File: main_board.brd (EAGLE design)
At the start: 160 x 100 mm, 8 parts, among them U1 MAX9019EKA+T

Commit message: working on the solar circuit
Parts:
- added C2: 10uF, MF_Passives:C0603
- added C3: 22uF, MF_Passives:C0603
- added J1: TBL009-254-02GY-2GY, PP_Connectors:TBL009-254-02GY-2GY
- added L1: 10uH, PP_Passives:LPS4012
- added R10, R7, R8, R9: (no value), MF_Passives:R0805
- added U2: AEM10941-QFN, PP_PowerIC:AEM10941_QFN-28
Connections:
- new net BOOST: C3.P$1, U2.P$1
- new net BUFSRC: C2.P$1, L1.P$2, U2.P$27
- new net SET_CHRDY: R8.P$2, R9.P$1, U2.P$23
- new net SET_OVCH: R10.P$1, R9.P$2, U2.P$22
- new net SET_OVDIS: R7.P$2, R8.P$1, U2.P$24
- new net SOLAR_+V: J1.1A, J1.1B, U2.P$25, U2.P$26
- new net SWBOOST: L1.P$1, U2.P$28
- new net VBOOST: R7.P$1
- net GND: now also C2.P$2, C3.P$2, J1.2A, J1.2B, R10.P$2

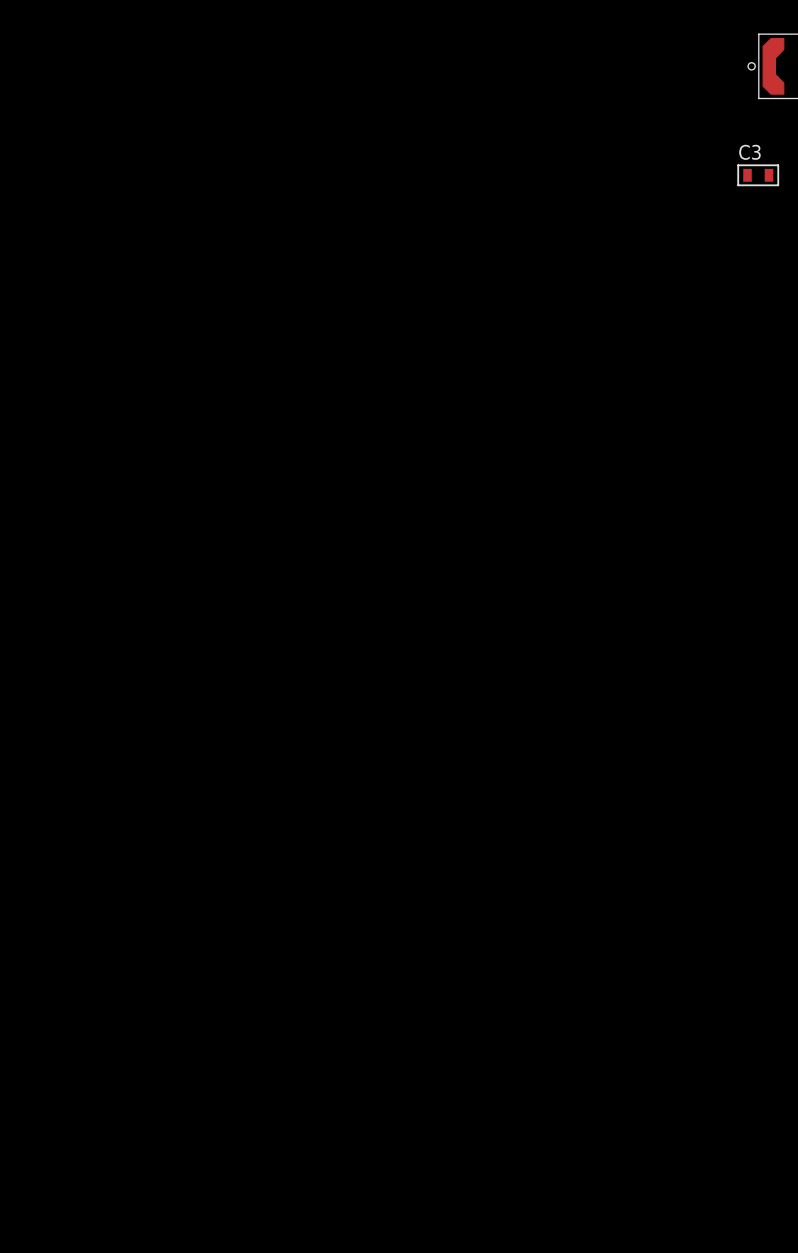
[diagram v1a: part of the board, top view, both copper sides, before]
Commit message: AEM10941 circuit complete
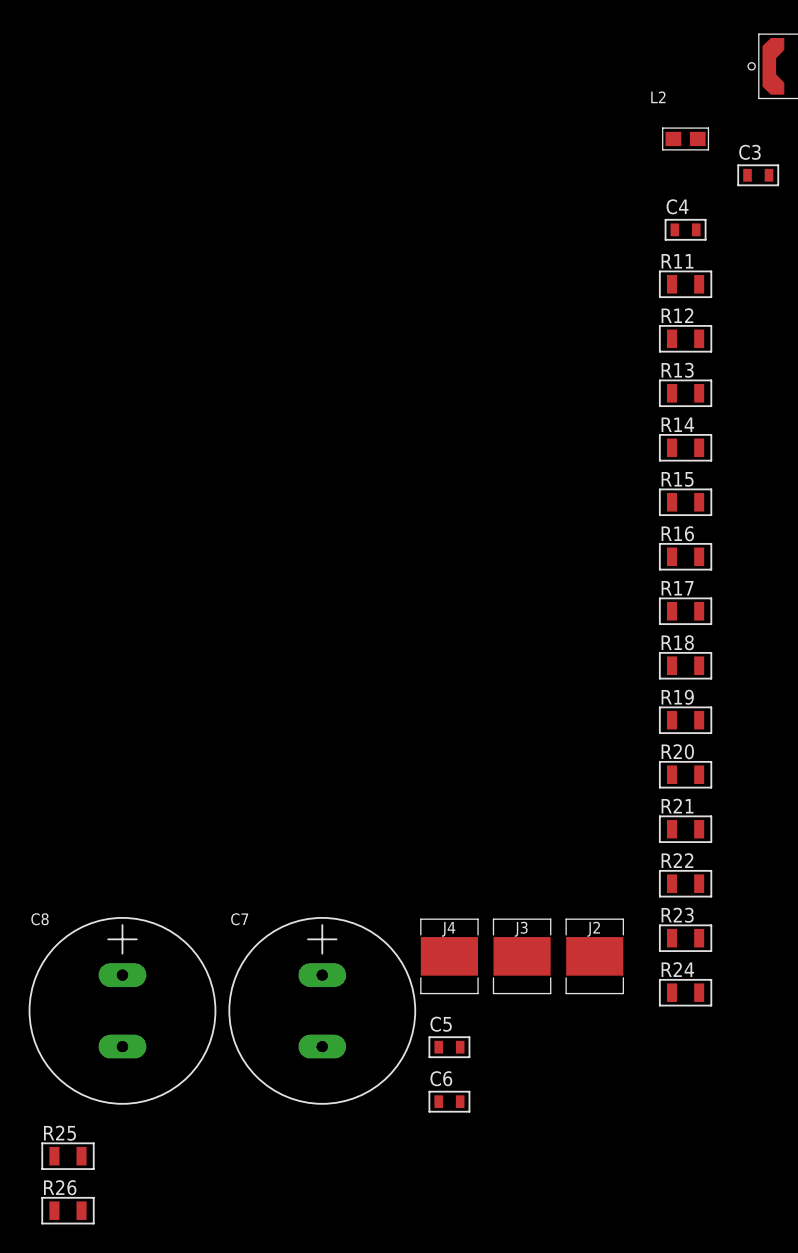
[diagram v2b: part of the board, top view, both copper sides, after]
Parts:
- added C4, C5, C6: 10uF, MF_Passives:C0603
- added C7, C8: 10F 3.8V, PP_Passives:12.5MM_CAP_PTH
- added J2, J3, J4: 709176001501006, PP_Connectors:709176001501006
- added L2: 10uH, PP_Passives:0603
- added R11, R12, R13, R14, R15, R16, R17, R18, R19, R20, R21, R22, R23, R24, R25, R26: (no value), MF_Passives:R0805
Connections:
- removed net BOOST: C3.P$1, U2.P$1
- new net BAL: C7.NEG, C8.POS, U2.P$15
- new net BATT: C7.POS, U2.P$16
- new net CFG[0]: R15.P$1, R16.P$2, U2.P$6
- new net CFG[1]: R13.P$1, R14.P$2, U2.P$5
- new net CFG[2]: R11.P$1, R12.P$2, U2.P$4
- new net ENHV: R21.P$1, R22.P$2, U2.P$12
- new net ENLV: R23.P$1, R24.P$2, U2.P$18
- new net FB_HV: R25.P$1, R26.P$2, U2.P$13
- new net HVOUT: C6.P$1, R25.P$2, U2.P$14
- new net LVOUT: C5.P$1, U2.P$11
- new net SELMPP[0]: R19.P$1, R20.P$2, U2.P$8
- new net SELMPP[1]: R17.P$1, R18.P$2, U2.P$7
- new net STATUS[0]: J4.P$1, U2.P$21
- new net STATUS[1]: J3.P$1, U2.P$20
- new net STATUS[2]: J2.P$1, U2.P$19
- new net SWBUCK: L2.1, U2.P$2
- new net VBUCK: C4.P$1, L2.2, R11.P$2, R13.P$2, R15.P$2, R17.P$2, R19.P$2, R21.P$2, R23.P$2, U2.P$3
- net GND: now also C4.P$2, C5.P$2, C6.P$2, C8.NEG, R12.P$1, R14.P$1, R16.P$1, R18.P$1, R20.P$1, R22.P$1, R24.P$1, R26.P$1, U2.P$10, U2.P$17, U2.P$29, U2.P$9
- net VBOOST: now also C3.P$1, U2.P$1

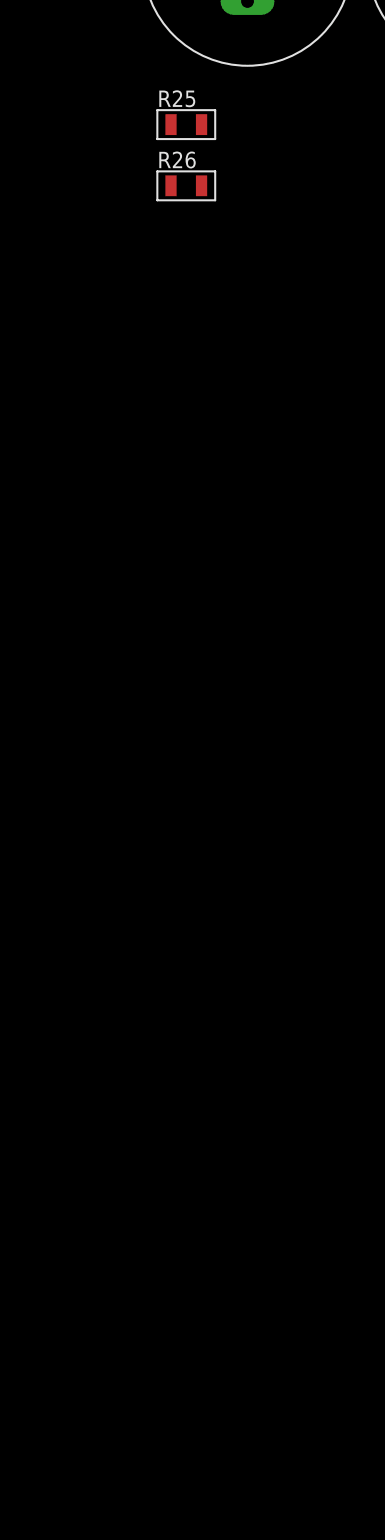
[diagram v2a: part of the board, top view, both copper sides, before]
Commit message: timer implemented in schematic
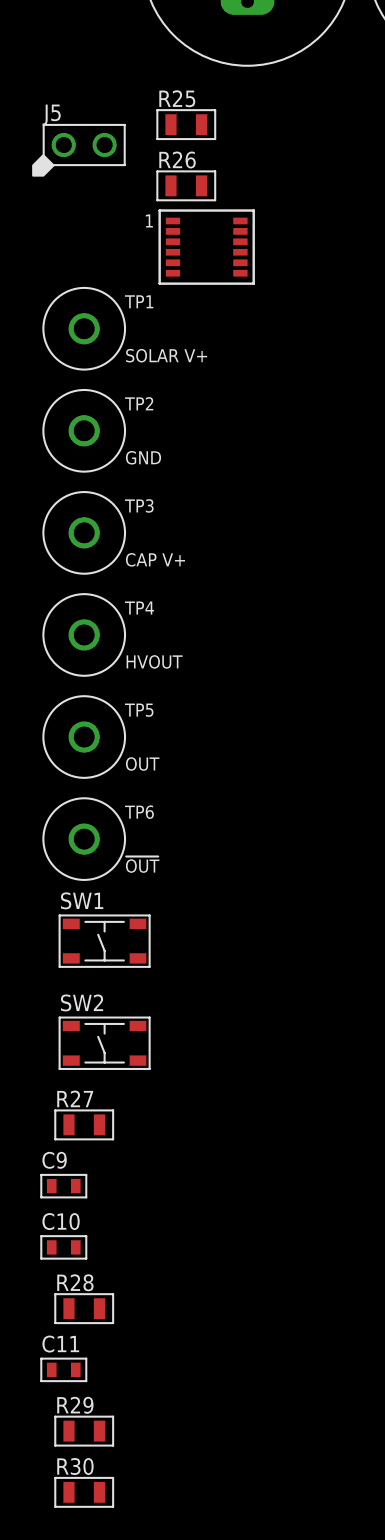
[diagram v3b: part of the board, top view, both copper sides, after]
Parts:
- added C10, C11, C9: 0.1uF, MF_Passives:C0603
- added J5: MF-CON-2.54mm-01x02, MF_Connectors:PTH_2.54MM_01X02
- added R27, R28: 100K, MF_Passives:R0805
- added R29: 162K, MF_Passives:R0805
- added R30: 121K, MF_Passives:R0805
- added SW1, SW2: (no value), MF_Switches:TACT4.2MM
- added TP1, TP2, TP3, TP4, TP5, TP6: 5115, PP_Connectors:KEYSTONE_5115-5119
- added U3: LTC2956IMS-1#PBF, PP_DigitalIC:LTC2956_MSOP-12
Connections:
- new net !OFFALERT: U3.P$10
- new net !ONALERT: U3.P$12
- new net !PB: SW1.P$4, U3.P$7
- new net !PBOUT: U3.P$9
- new net !SLEEP: C10.P$1, R27.P$2, SW2.P$1, U3.P$11
- new net EN: U3.P$8
- new net LONG: R28.P$1, U3.P$2
- new net PERIOD: R30.P$2, U3.P$4
- new net RANGE: R28.P$2, R29.P$2, U3.P$3
- net !OUT: now also TP6.P$1
- net 3.3V: now also C11.P$1, C9.P$1, J5.P$1, SW2.P$4, U3.P$5
- net BATT: now also TP3.P$1
- net GND: now also C10.P$2, C11.P$2, C9.P$2, R27.P$1, R29.P$1, R30.P$1, SW1.P$1, TP2.P$1, U3.P$1, U3.P$6
- net HVOUT: now also J5.P$2, TP4.P$1
- net OUT: now also TP5.P$1
- net SOLAR_+V: now also TP1.P$1
